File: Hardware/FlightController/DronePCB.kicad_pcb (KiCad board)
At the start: 2 copper layers, 53.1 x 93.3 mm, 15 parts, among them U1 ESP32-DEVKIT-V1

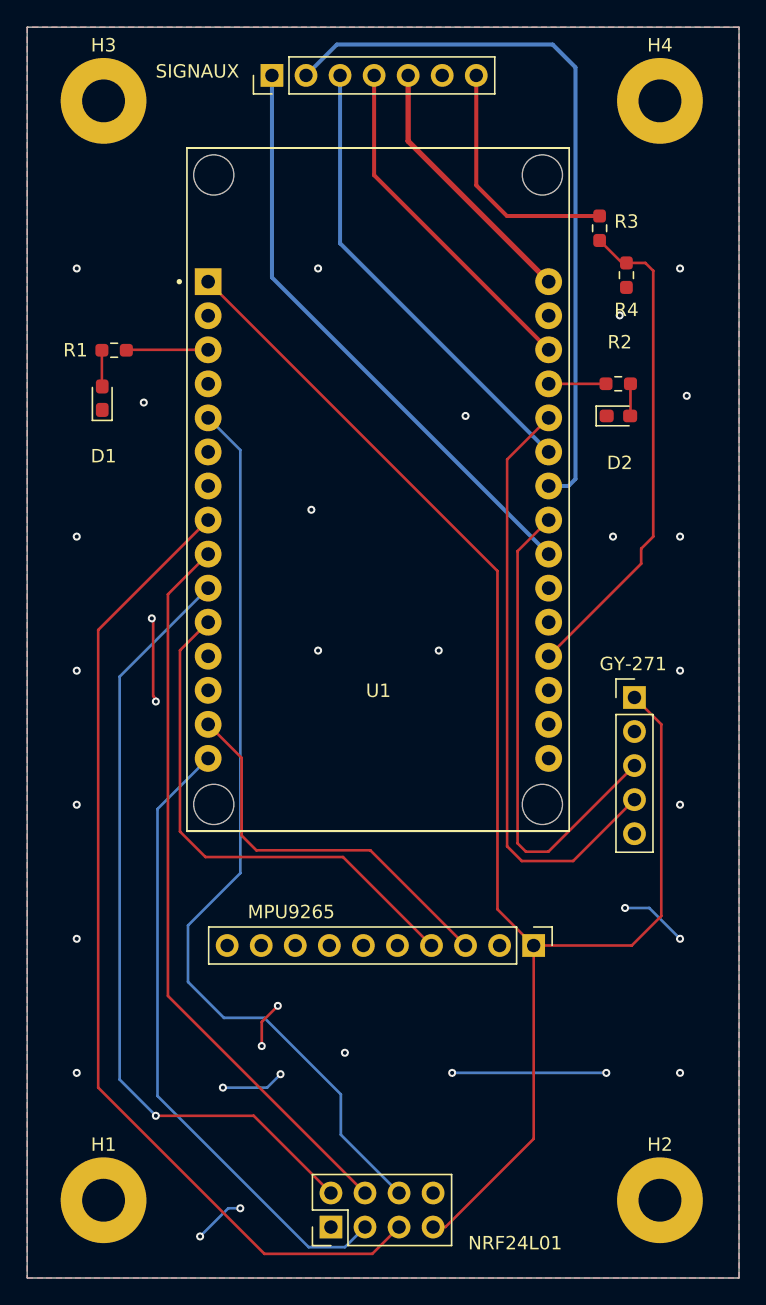
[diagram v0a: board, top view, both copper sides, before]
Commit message: PCB avec nouveau connecteur JST SH + buffer
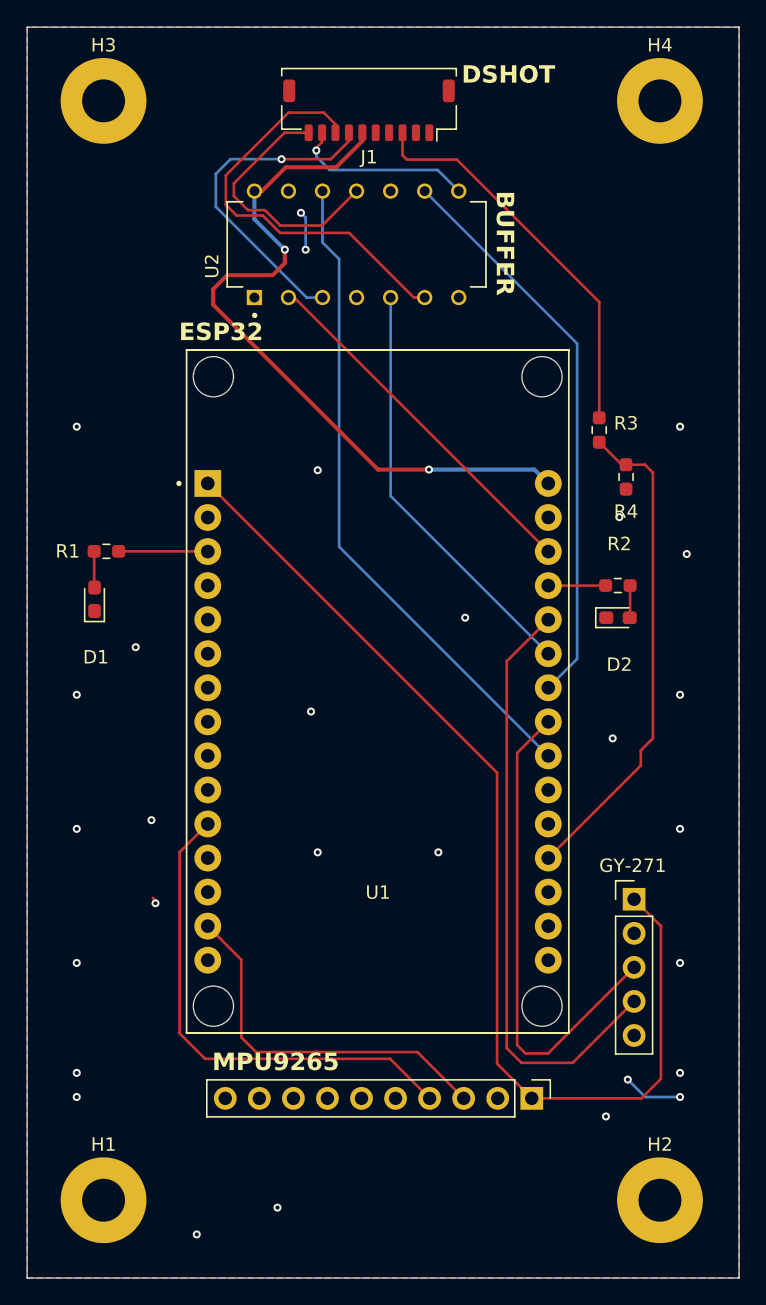
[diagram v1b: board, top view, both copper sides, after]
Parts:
- removed NRF24L01: Conn_02x04_Odd_Even, Connector_PinHeader_2.54mm:PinHeader_2x04_P2.54mm_Vertical
- removed SIGNAUX: Conn_01x07_Pin, Connector_PinHeader_2.54mm:PinHeader_1x07_P2.54mm_Vertical
- added J1: ESC SIGNALS, Connector_JST:JST_SHL_SM10B-SHLS-TF_1x10-1MP_P1.00mm_Horizontal, F.Cu at (41.8, 23.2)
- added U2: SN74AHCT125N, SN74AHCT125N_FP:DIP794W45P254L1930H508Q14, F.Cu at (40.9, 33.2)
- moved D2 15.1 mm to (60.4, 61.0)
- moved GY-271 15.1 mm to (61.6, 82.0)
- moved R2 15.1 mm to (60.4, 58.6)
- moved R3 15.1 mm to (59.0, 47.0)
- moved R4 15.1 mm to (61.0, 50.5)
- moved U1 15.1 mm to (42.5, 66.5)
- moved D1 15.0 mm to (21.3, 59.7)
- moved R1 15.0 mm to (22.2, 56.1)
- moved MPU9265 11.4 mm to (53.9, 96.9)
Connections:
- U1 pad 10: MISO -> unconnected-(U1-D19-Pad10)
- U1 pad 15: MOSI -> unconnected-(U1-D23-Pad15)
- U1 pad 22: Moteur4 -> MoteurA4
- U1 pad 24: Moteur3 -> MoteurA3
- U1 pad 25: Moteur2 -> MoteurA2
- U1 pad 28: Moteur1 -> MoteurA1
- U1 pad 5: NRF_CE -> unconnected-(U1-D4-Pad5)
- U1 pad 8: NRF_CSN -> unconnected-(U1-D5-Pad8)
- U1 pad 9: SCK -> unconnected-(U1-D18-Pad9)
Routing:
- net NRF_CSN: track 74.1 -> 0.00 mm
- net NRF_CE: track 68.7 -> 0.00 mm
- net MISO: track 58.7 -> 0.00 mm, vias 1 -> 0
- net SCK: track 55.0 -> 0.00 mm
- net Moteur3: track 54.7 -> 0.00 mm
- net MoteurA4: track 0.00 -> 49.1 mm
- net MOSI: track 47.5 -> 0.00 mm
- net Moteur4: track 44.3 -> 0.00 mm
- net MoteurA3: track 0.00 -> 42.6 mm
- net BEC_5V: track 19.7 -> 54.4 mm, vias 0 -> 2
- net Moteur2: track 34.5 -> 0.00 mm
- net 3V3: track 111.8 -> 80.3 mm
- net MoteurA2: track 0.00 -> 31.4 mm
- net MoteurY2: track 0.00 -> 31.0 mm
- net MoteurA1: track 0.00 -> 27.2 mm
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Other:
- board text added: "BUFFER"
- board text added: "DSHOT"
- board text added: "ESP32"
- board text added: "MPU9265"
